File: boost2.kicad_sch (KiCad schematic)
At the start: 33 parts, among them Q8 BSC059N04LS6, Q9 BSC059N04LS6, U17 TPS43061

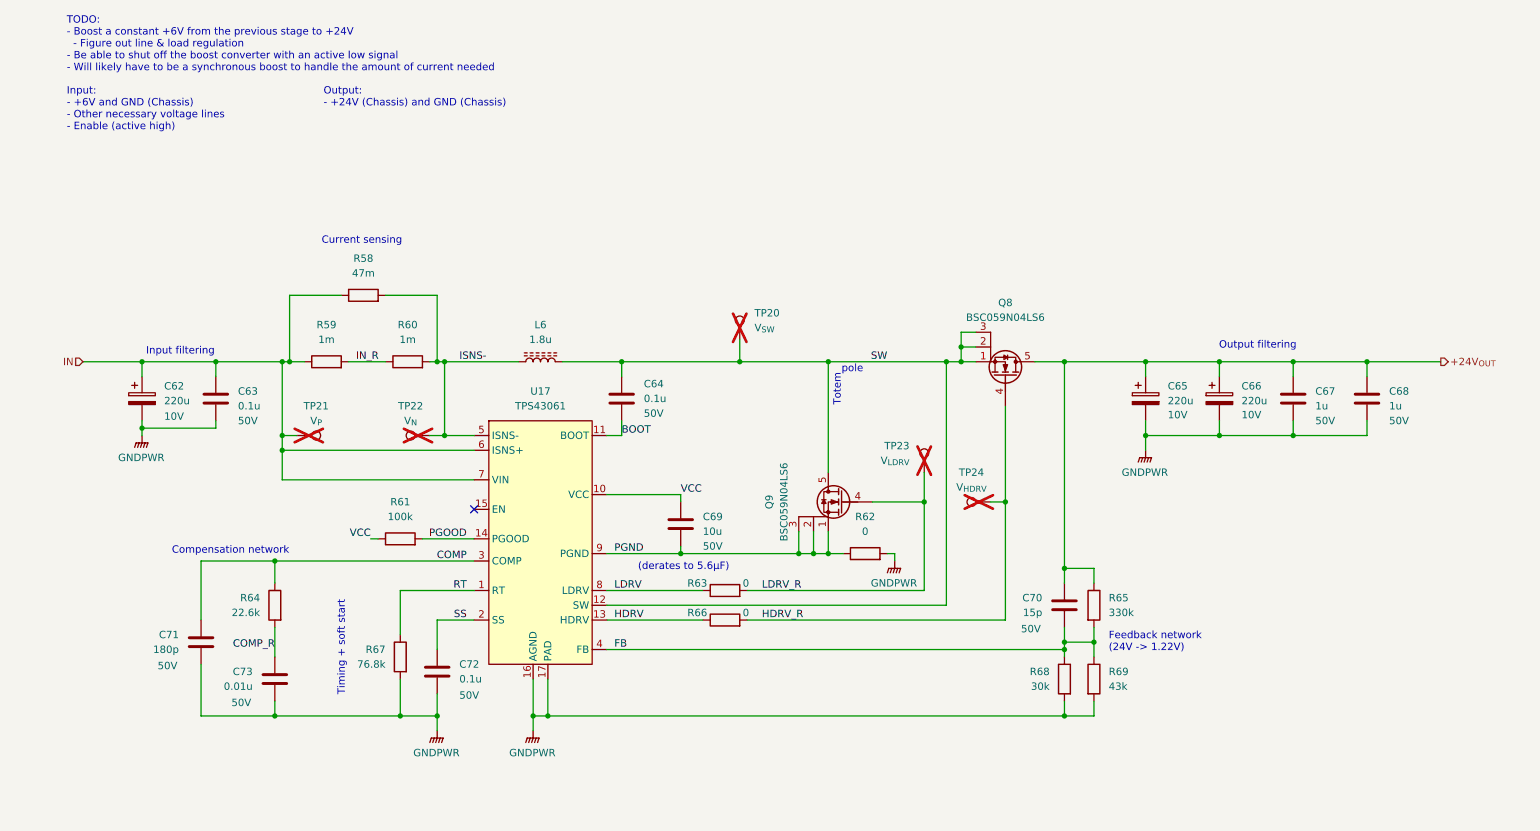
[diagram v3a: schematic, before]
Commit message: Begin layout
Completed ideal diode layout
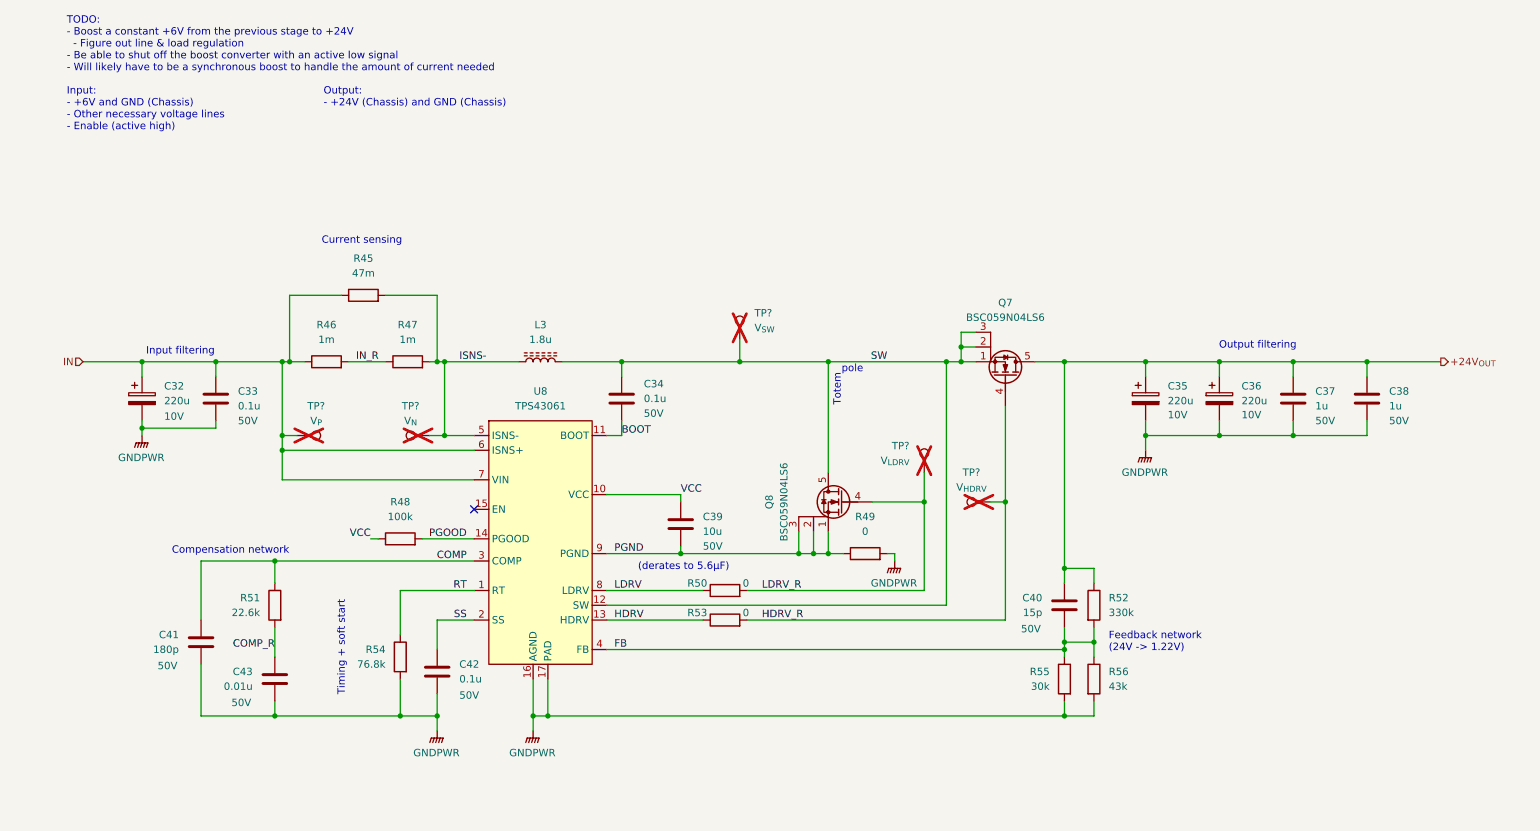
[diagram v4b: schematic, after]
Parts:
- renumbered C62 to C32, C63 to C33, C64 to C34, C65 to C35, C66 to C36, C67 to C37, C68 to C38, C69 to C39, C70 to C40, C71 to C41, C72 to C42, C73 to C43, L6 to L3, Q8 to Q7, Q9 to Q8, R58 to R45, R59 to R46, R60 to R47, R61 to R48, R62 to R49, R63 to R50, R64 to R51, R65 to R52, R66 to R53, R67 to R54, R68 to R55, R69 to R56, TP20 to TP?, TP21 to TP?, TP23 to TP?, TP24 to TP?, TP22 to TP?, U17 to U8
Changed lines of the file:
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@@
 		(on_board yes)
 		(dnp no)
-		(property "Reference" "C62"
+		(property "Reference" "C32"
 			(at 40.64 84.2009 0)
 			(effects
@@
 		(on_board yes)
 		(dnp no)
-		(property "Reference" "C67"
+		(property "Reference" "C37"
 			(at 238.76 85.0899 0)
 			(effects
@@
 		(on_board yes)
 		(dnp no)
-		(property "Reference" "C66"
+		(property "Reference" "C36"
 			(at 226.06 84.2009 0)
 			(effects
@@
 		(dnp no)
 		(fields_autoplaced yes)
-		(property "Reference" "R62"
+		(property "Reference" "R49"
 			(at 161.29 106.68 90)
 			(effects
@@
 		(dnp no)
 		(fields_autoplaced yes)
-		(property "Reference" "R61"
+		(property "Reference" "R48"
 			(at 81.28 104.14 90)
 			(effects
@@
 		(dnp no)
 		(fields_autoplaced yes)
-		(property "Reference" "R59"
+		(property "Reference" "R46"
 			(at 68.58 73.66 90)
 			(effects
@@
 		(dnp no)
 		(fields_autoplaced yes)
-		(property "Reference" "#PWR0113"
+		(property "Reference" "#PWR054"
 			(at 36.83 97.79 0)
 			(effects
@@
 		(dnp no)
 		(fields_autoplaced yes)
-		(property "Reference" "#PWR0117"
+		(property "Reference" "#PWR058"
 			(at 104.14 148.59 0)
 			(effects
@@
 		(dnp yes)
 		(fields_autoplaced yes)
-		(property "Reference" "TP20"
+		(property "Reference" "TP?"
 			(at 142.24 71.6279 0)
 			(effects
@@
 		)
 		(instances
+			(project "SupercapManager"
+				(path "/6197145b-e7d4-44cc-9d90-537b6501bf60/47dffa6f-2678-4be2-969a-7f2e7310ccad"
+					(reference "TP?")
+					(unit 1)
+				)
+			)
 			(project "Rev 1B"
 				(path "/e5f99deb-ef42-4c5f-b80a-388477910e20/d2569310-1133-4585-8eb3-8b8cc99091a2"
@@
 		(on_board yes)
 		(dnp no)
-		(property "Reference" "C72"
+		(property "Reference" "C42"
 			(at 91.44 132.0799 0)
 			(effects
@@
 		(on_board yes)
 		(dnp yes)
-		(property "Reference" "TP21"
+		(property "Reference" "TP?"
 			(at 66.802 87.63 90)
 			(effects
@@
 		)
 		(instances
+			(project "SupercapManager"
+				(path "/6197145b-e7d4-44cc-9d90-537b6501bf60/47dffa6f-2678-4be2-969a-7f2e7310ccad"
+					(reference "TP?")
+					(unit 1)
+				)
+			)
 			(project "Rev 1B"
 				(path "/e5f99deb-ef42-4c5f-b80a-388477910e20/d2569310-1133-4585-8eb3-8b8cc99091a2"
@@
 		(on_board yes)
 		(dnp no)
-		(property "Reference" "R68"
+		(property "Reference" "R55"
 			(at 193.04 133.3499 0)
 			(effects
@@
 		(on_board yes)
 		(dnp no)
-		(property "Reference" "Q9"
+		(property "Reference" "Q8"
 			(at 144.78 104.14 90)
 			(effects
@@
 		(on_board yes)
 		(dnp no)
-		(property "Reference" "Q8"
+		(property "Reference" "Q7"
 			(at 185.42 69.85 90)
 			(effects
@@
 		(dnp no)
 		(fields_autoplaced yes)
-		(property "Reference" "#PWR0116"
+		(property "Reference" "#PWR057"
 			(at 87.63 148.59 0)
 			(effects
@@
 		(on_board yes)
 		(dnp no)
-		(property "Reference" "R67"
+		(property "Reference" "R54"
 			(at 78.74 129.5399 0)
 			(effects
@@
 		(on_board yes)
 		(dnp no)
-		(property "Reference" "R64"
+		(property "Reference" "R51"
 			(at 57.15 120.6499 0)
 			(effects
@@
 		(on_board yes)
 		(dnp yes)
-		(property "Reference" "TP23"
+		(property "Reference" "TP?"
 			(at 168.91 94.4879 0)
 			(effects
@@
 		)
 		(instances
+			(project "SupercapManager"
+				(path "/6197145b-e7d4-44cc-9d90-537b6501bf60/47dffa6f-2678-4be2-969a-7f2e7310ccad"
+					(reference "TP?")
+					(unit 1)
+				)
+			)
 			(project "Rev 1B"
 				(path "/e5f99deb-ef42-4c5f-b80a-388477910e20/d2569310-1133-4585-8eb3-8b8cc99091a2"
@@
 		(dnp no)
 		(fields_autoplaced yes)
-		(property "Reference" "#PWR0114"
+		(property "Reference" "#PWR055"
 			(at 209.55 100.33 0)
 			(effects
@@
 		(on_board yes)
 		(dnp no)
-		(property "Reference" "C68"
+		(property "Reference" "C38"
 			(at 251.46 85.0899 0)
 			(effects
@@
 		(on_board yes)
 		(dnp no)
-		(property "Reference" "C73"
+		(property "Reference" "C43"
 			(at 55.88 133.3499 0)
 			(effects
@@
 		(on_board yes)
 		(dnp no)
-		(property "Reference" "C63"
+		(property "Reference" "C33"
 			(at 53.34 85.0899 0)
 			(effects
@@
 		(on_board yes)
 		(dnp no)
-		(property "Reference" "R63"
+		(property "Reference" "R50"
 			(at 134.112 118.872 90)
 			(effects
@@
 		(on_board yes)
 		(dnp no)
-		(property "Reference" "C69"
+		(property "Reference" "C39"
 			(at 133.35 106.6799 0)
 			(effects
@@
 		(dnp no)
 		(fields_autoplaced yes)
-		(property "Reference" "R58"
+		(property "Reference" "R45"
 			(at 74.93 62.23 90)
 			(effects
@@
 		(dnp yes)
 		(fields_autoplaced yes)
-		(property "Reference" "TP24"
+		(property "Reference" "TP?"
 			(at 179.578 99.06 90)
 			(effects
@@
 		)
 		(instances
+			(project "SupercapManager"
+				(path "/6197145b-e7d4-44cc-9d90-537b6501bf60/47dffa6f-2678-4be2-969a-7f2e7310ccad"
+					(reference "TP?")
+					(unit 1)
+				)
+			)
 			(project "Rev 1B"
 				(path "/e5f99deb-ef42-4c5f-b80a-388477910e20/d2569310-1133-4585-8eb3-8b8cc99091a2"
@@
 		(dnp no)
 		(fields_autoplaced yes)
-		(property "Reference" "U17"
+		(property "Reference" "U8"
 			(at 105.41 85.09 0)
 			(effects
@@
 		(on_board yes)
 		(dnp no)
-		(property "Reference" "C70"
+		(property "Reference" "C40"
 			(at 191.77 120.6499 0)
 			(effects
@@
 		(on_board yes)
 		(dnp no)
-		(property "Reference" "R66"
+		(property "Reference" "R53"
 			(at 134.112 123.952 90)
 			(effects
@@
 		(dnp no)
 		(fields_autoplaced yes)
-		(property "Reference" "#PWR0115"
+		(property "Reference" "#PWR056"
 			(at 166.37 119.38 0)
 			(effects
@@
 		(dnp no)
 		(fields_autoplaced yes)
-		(property "Reference" "R60"
+		(property "Reference" "R47"
 			(at 82.55 73.66 90)
 			(effects
@@
 		(on_board yes)
 		(dnp no)
-		(property "Reference" "C64"
+		(property "Reference" "C34"
 			(at 123.19 83.82 0)
 			(effects
@@
 		(on_board yes)
 		(dnp no)
-		(property "Reference" "C65"
+		(property "Reference" "C35"
 			(at 213.36 84.2009 0)
 			(effects
@@
 		(dnp no)
 		(fields_autoplaced yes)
-		(property "Reference" "R69"
+		(property "Reference" "R56"
 			(at 203.2 133.3499 0)
 			(effects
@@
 		(dnp no)
 		(fields_autoplaced yes)
-		(property "Reference" "L6"
+		(property "Reference" "L3"
 			(at 105.41 73.66 90)
 			(effects
@@
 		(on_board yes)
 		(dnp no)
-		(property "Reference" "C71"
+		(property "Reference" "C41"
 			(at 43.18 126.9999 0)
 			(effects
@@
 		(on_board yes)
 		(dnp yes)
-		(property "Reference" "TP22"
+		(property "Reference" "TP?"
 			(at 83.058 87.63 90)
 			(effects
@@
 		)
 		(instances
+			(project "SupercapManager"
+				(path "/6197145b-e7d4-44cc-9d90-537b6501bf60/47dffa6f-2678-4be2-969a-7f2e7310ccad"
+					(reference "TP?")
+					(unit 1)
+				)
+			)
 			(project "Rev 1B"
 				(path "/e5f99deb-ef42-4c5f-b80a-388477910e20/d2569310-1133-4585-8eb3-8b8cc99091a2"
@@
 		(dnp no)
 		(fields_autoplaced yes)
-		(property "Reference" "R65"
+		(property "Reference" "R52"
 			(at 203.2 120.6499 0)
 			(effects

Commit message: Add input filter to Boost 2
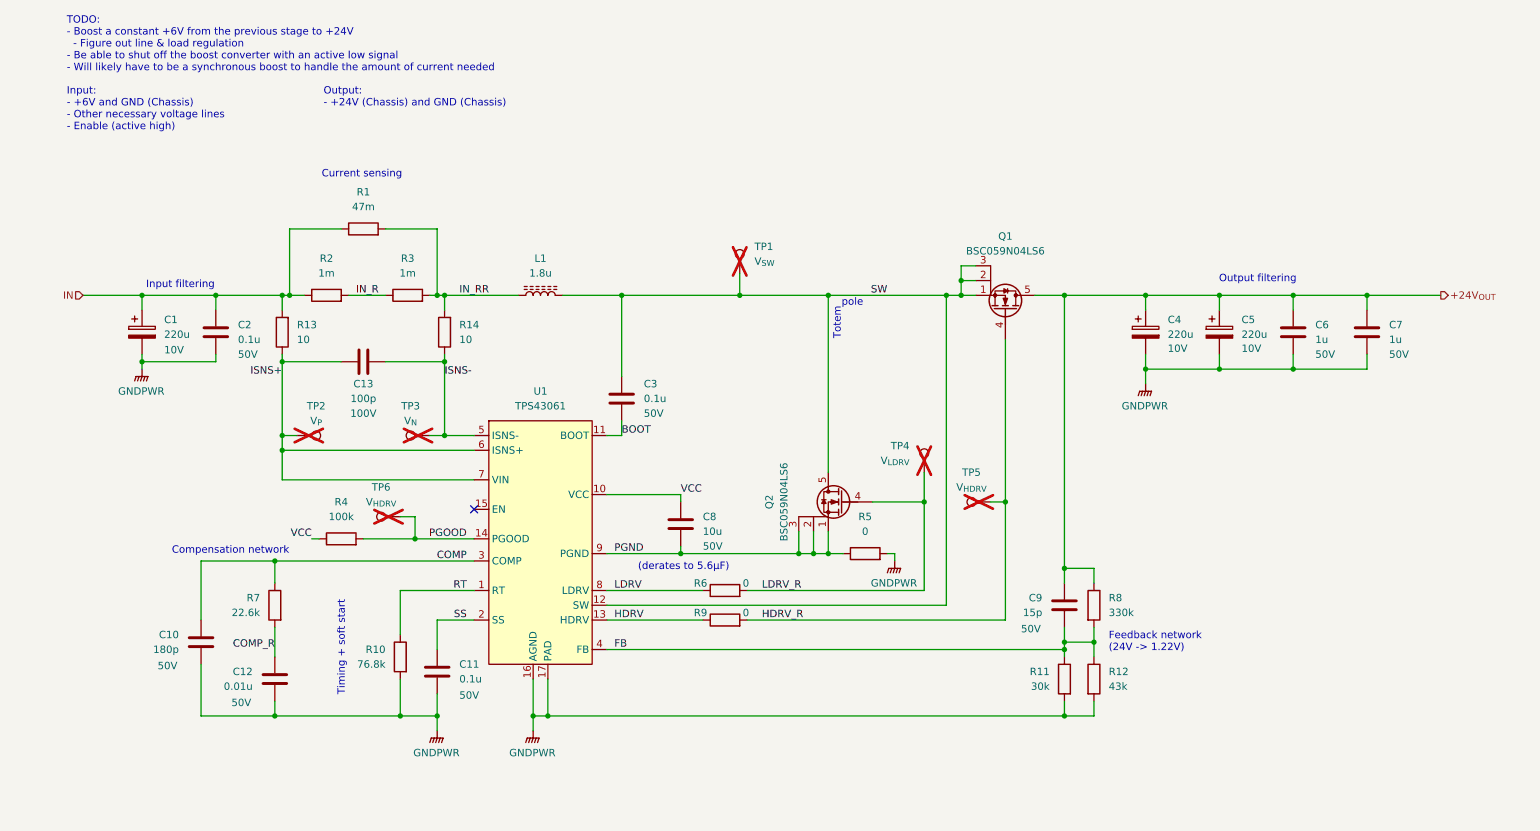
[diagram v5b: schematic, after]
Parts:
- added C13: 100p, Capacitor_SMD:C_0603_1608Metric_Pad1.08x0.95mm_HandSolder, symbol Device:C
- added R13, R14: 10, Resistor_SMD:R_0603_1608Metric_Pad0.98x0.95mm_HandSolder, symbol Device:R
- added TP6: V_{HDRV}, TestPoint:TestPoint_Bridge_Pitch2.0mm_Drill0.7mm, symbol Connector:TestPoint
- gave numbers to parts that had none: 5
- renumbered C32 to C1, C41 to C10, C42 to C11, C43 to C12, C33 to C2, C34 to C3, C35 to C4, C36 to C5, C37 to C6, C38 to C7, C39 to C8, C40 to C9, L3 to L1, Q7 to Q1, Q8 to Q2, R45 to R1, R54 to R10, R55 to R11, R56 to R12, R46 to R2, R47 to R3, R48 to R4, R49 to R5, R50 to R6, R51 to R7, R52 to R8, R53 to R9, U8 to U1
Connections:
- net IN: now also R13.2; no longer TP2.1, U1.6 (ISNS+), U1.7 (VIN)
- net ISNS-: now also C13.2, R14.1; no longer L1.1, R1.2, R3.2
- net PGOOD: now also TP6.1
- new net IN_RR: L1.1, R1.2, R14.2, R3.2
- new net ISNS+: C13.1, R13.1, TP2.1, U1.6 (ISNS+), U1.7 (VIN)
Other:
- moved on the sheet: C1, C2, C4, C5, C6, C7, L1, Q1, R1, R2, R3, R4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

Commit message: Complete boost2 layout
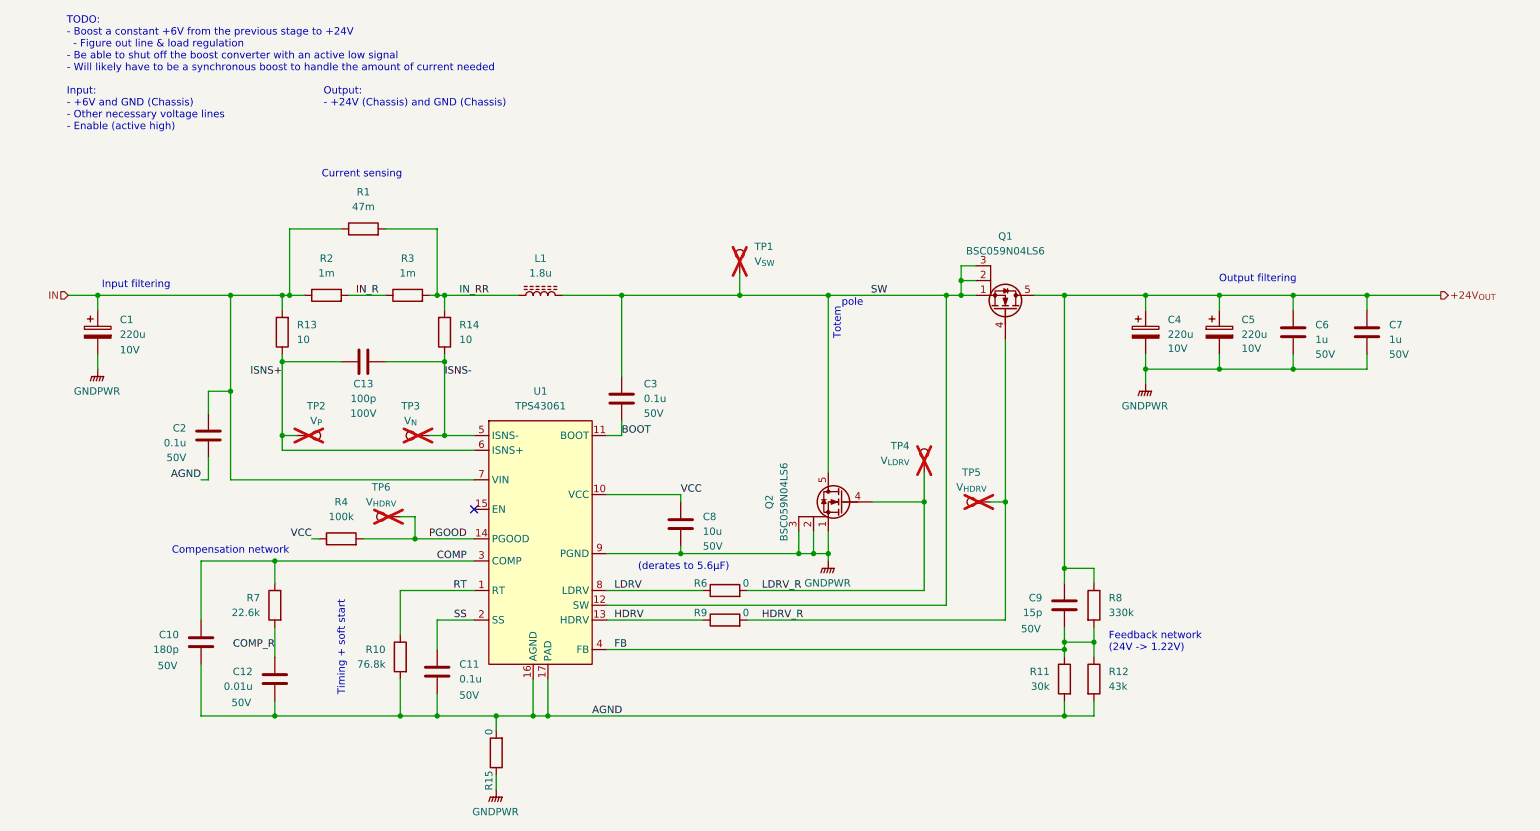
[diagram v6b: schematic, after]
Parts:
- removed R5: 0, Resistor_SMD:R_0603_1608Metric_Pad0.98x0.95mm_HandSolder, symbol Device:R
- added R15: 0, Resistor_SMD:R_0603_1608Metric_Pad0.98x0.95mm_HandSolder, symbol Device:R
- TP2, TP3, TP4, TP5: footprint TestPoint:TestPoint_Bridge_Pitch2.0mm_Drill0.7mm -> TestPoint:TestPoint_Pad_1.0x1.0mm
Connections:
- net PGND is gone; now on net GNDPWR: C8.2, Q2.1 (S), Q2.2 (S), Q2.3 (S), U1.9 (PGND)
- net GNDPWR: now also R15.1; no longer C10.2, C11.2, C12.2, C2.2, R10.2, R11.2, R12.2, U1.16 (AGND), U1.17 (PAD)
- net IN: now also U1.7 (VIN)
- net ISNS+: no longer U1.7 (VIN)
- new net AGND: C10.2, C11.2, C12.2, C2.2, R10.2, R11.2, R12.2, R15.2, U1.16 (AGND), U1.17 (PAD)
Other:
- moved on the sheet: C1, C2
